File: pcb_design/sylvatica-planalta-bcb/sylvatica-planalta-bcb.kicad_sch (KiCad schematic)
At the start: 5 parts, among them J1 USB_C_Receptacle, J2 Conn_02x07_Odd_Even, J3 USB_C_Receptacle, J4 Conn_01x06

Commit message: Gerber exports
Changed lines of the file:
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@@
+    (stroke (width 0) (type default) (color 0 0 0 0))
+  )
+  (wire (pts (xy 198.12 106.68) (xy 207.01 106.68))
     (stroke (width 0) (type default) (color 0 0 0 0))
   )
@@
   )
   (wire (pts (xy 114.3 88.9) (xy 123.19 88.9))
+    (stroke (width 0) (type default) (color 0 0 0 0))
+  )
+  (wire (pts (xy 198.12 97.79) (xy 207.01 97.79))
     (stroke (width 0) (type default) (color 0 0 0 0))
   )
@@
     (pin "9")
   )
+  (symbol (lib_id "power:PWR_FLAG") (at 207.01 114.3 0) (unit 1)
+    (in_bom yes) (on_board yes) (fields_autoplaced)
+    (property "Reference" "#FLG0102" (id 0) (at 207.01 112.395 0)
+      (effects (font (size 1.27 1.27)) hide)
+    )
+    (property "Value" "PWR_FLAG" (id 1) (at 207.01 109.22 0))
+    (property "Footprint" "" (id 2) (at 207.01 114.3 0)
+      (effects (font (size 1.27 1.27)) hide)
+    )
+    (property "Datasheet" "~" (id 3) (at 207.01 114.3 0)
+      (effects (font (size 1.27 1.27)) hide)
+    )
+    (pin "1")
+  )
   (symbol (lib_id "power:VBUS") (at 123.19 83.82 0) (unit 1)
     (in_bom yes) (on_board yes) (fields_autoplaced)
@@
     )
     (property "Datasheet" "" (id 3) (at 123.19 83.82 0)
+      (effects (font (size 1.27 1.27)) hide)
+    )
+    (pin "1")
+  )
+  (symbol (lib_id "power:PWR_FLAG") (at 207.01 97.79 0) (unit 1)
+    (in_bom yes) (on_board yes) (fields_autoplaced)
+    (property "Reference" "#FLG0103" (id 0) (at 207.01 95.885 0)
+      (effects (font (size 1.27 1.27)) hide)
+    )
+    (property "Value" "PWR_FLAG" (id 1) (at 207.01 92.71 0))
+    (property "Footprint" "" (id 2) (at 207.01 97.79 0)
+      (effects (font (size 1.27 1.27)) hide)
+    )
+    (property "Datasheet" "~" (id 3) (at 207.01 97.79 0)
+      (effects (font (size 1.27 1.27)) hide)
+    )
+    (pin "1")
+  )
+  (symbol (lib_id "power:GND") (at 207.01 114.3 0) (unit 1)
+    (in_bom yes) (on_board yes) (fields_autoplaced)
+    (property "Reference" "#PWR0110" (id 0) (at 207.01 120.65 0)
+      (effects (font (size 1.27 1.27)) hide)
+    )
+    (property "Value" "GND" (id 1) (at 207.01 119.38 0))
+    (property "Footprint" "" (id 2) (at 207.01 114.3 0)
+      (effects (font (size 1.27 1.27)) hide)
+    )
+    (property "Datasheet" "" (id 3) (at 207.01 114.3 0)
       (effects (font (size 1.27 1.27)) hide)
     )
@@
     (pin "6")
   )
+  (symbol (lib_id "power:VBUS") (at 198.12 106.68 0) (unit 1)
+    (in_bom yes) (on_board yes) (fields_autoplaced)
+    (property "Reference" "#PWR0109" (id 0) (at 198.12 110.49 0)
+      (effects (font (size 1.27 1.27)) hide)
+    )
+    (property "Value" "VBUS" (id 1) (at 198.12 101.6 0))
+    (property "Footprint" "" (id 2) (at 198.12 106.68 0)
+      (effects (font (size 1.27 1.27)) hide)
+    )
+    (property "Datasheet" "" (id 3) (at 198.12 106.68 0)
+      (effects (font (size 1.27 1.27)) hide)
+    )
+    (pin "1")
+  )
   (symbol (lib_id "power:GND") (at 95.25 149.86 0) (unit 1)
     (in_bom yes) (on_board yes) (fields_autoplaced)
@@
     )
     (property "Datasheet" "" (id 3) (at 86.36 52.07 0)
+      (effects (font (size 1.27 1.27)) hide)
+    )
+    (pin "1")
+  )
+  (symbol (lib_id "power:PWR_FLAG") (at 207.01 106.68 0) (unit 1)
+    (in_bom yes) (on_board yes) (fields_autoplaced)
+    (property "Reference" "#FLG0101" (id 0) (at 207.01 104.775 0)
+      (effects (font (size 1.27 1.27)) hide)
+    )
+    (property "Value" "PWR_FLAG" (id 1) (at 207.01 101.6 0))
+    (property "Footprint" "" (id 2) (at 207.01 106.68 0)
+      (effects (font (size 1.27 1.27)) hide)
+    )
+    (property "Datasheet" "~" (id 3) (at 207.01 106.68 0)
+      (effects (font (size 1.27 1.27)) hide)
+    )
+    (pin "1")
+  )
+  (symbol (lib_id "power:+3.3V") (at 198.12 97.79 0) (unit 1)
+    (in_bom yes) (on_board yes) (fields_autoplaced)
+    (property "Reference" "#PWR0111" (id 0) (at 198.12 101.6 0)
+      (effects (font (size 1.27 1.27)) hide)
+    )
+    (property "Value" "+3.3V" (id 1) (at 198.12 92.71 0))
+    (property "Footprint" "" (id 2) (at 198.12 97.79 0)
+      (effects (font (size 1.27 1.27)) hide)
+    )
+    (property "Datasheet" "" (id 3) (at 198.12 97.79 0)
       (effects (font (size 1.27 1.27)) hide)
     )
@@
   )
   (symbol_instances
+    (path "/c01fd3c1-dfa9-46f7-a6b5-5f8ffe94637d"
+      (reference "#FLG0101") (unit 1) (value "PWR_FLAG") (footprint "")
+    )
+    (path "/73bb7407-42d7-48e9-99a3-b7d5d2bb2d1d"
+      (reference "#FLG0102") (unit 1) (value "PWR_FLAG") (footprint "")
+    )
+    (path "/93363c7c-e290-4fbd-ae52-8d881948c1c3"
+      (reference "#FLG0103") (unit 1) (value "PWR_FLAG") (footprint "")
+    )
     (path "/e31f94a3-1f71-4323-bf6e-1b3f93eeed91"
       (reference "#PWR01") (unit 1) (value "+3.3V") (footprint "")
@@
       (reference "#PWR0108") (unit 1) (value "VBUS") (footprint "")
     )
+    (path "/a5485afb-82c9-4956-9d49-d1277136f874"
+      (reference "#PWR0109") (unit 1) (value "VBUS") (footprint "")
+    )
+    (path "/941fe0bb-3818-48e0-a99d-ae1994cf3cb3"
+      (reference "#PWR0110") (unit 1) (value "GND") (footprint "")
+    )
+    (path "/c4b96c0e-e6e5-4d46-8fac-385633c2366c"
+      (reference "#PWR0111") (unit 1) (value "+3.3V") (footprint "")
+    )
     (path "/dc37d966-d882-4451-ba5d-342ef3a9987e"

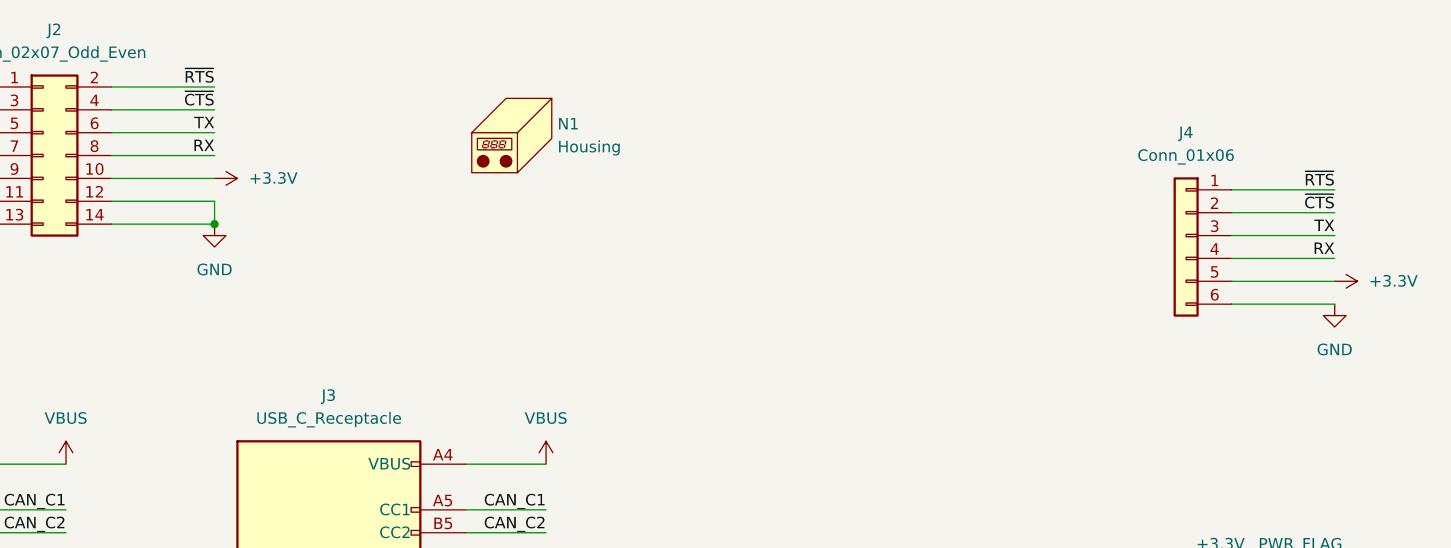
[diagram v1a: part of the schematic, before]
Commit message: Expose RTCC pin for synchronisation
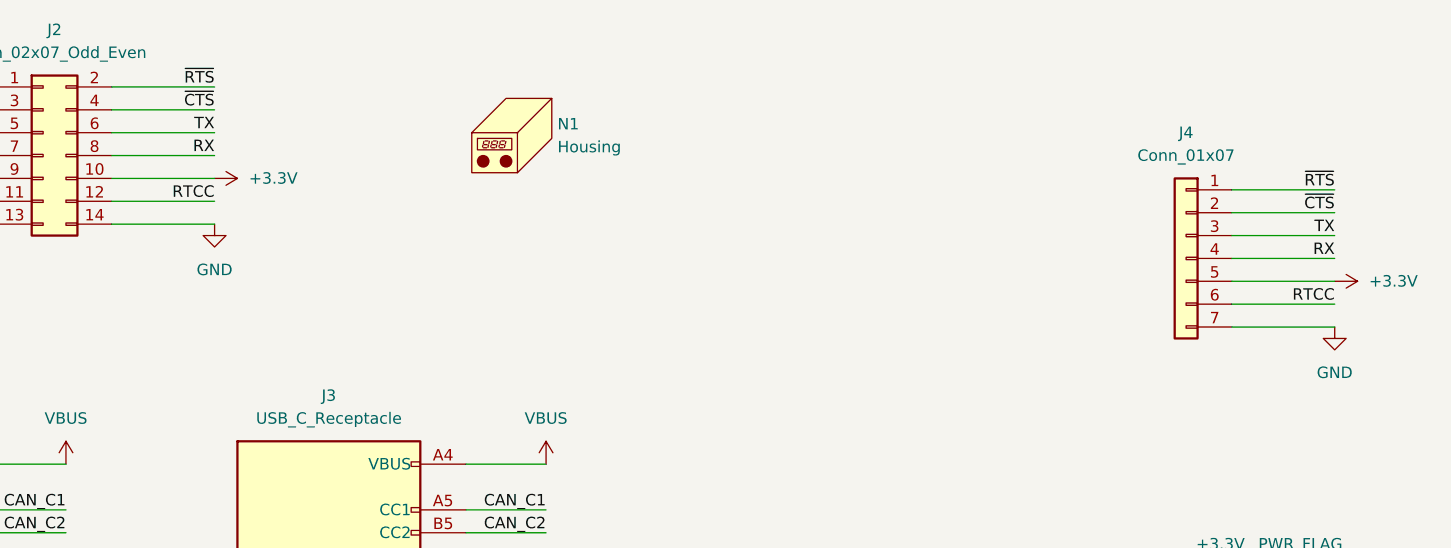
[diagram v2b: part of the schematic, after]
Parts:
- removed J4: Conn_01x06, Connector_PinHeader_2.54mm:PinHeader_1x06_P2.54mm_Vertical, symbol Connector_Generic:Conn_01x06
- added J4: Conn_01x07, Connector_PinHeader_2.54mm:PinHeader_1x07_P2.54mm_Vertical, symbol Connector_Generic:Conn_01x07
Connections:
- net +3.3V: now also J4.5 (Pin_5)
- net GND: now also J4.7 (Pin_7); no longer J2.12 (Pin_12)
- net RX: now also J4.4 (Pin_4)
- net TX: now also J4.3 (Pin_3)
- net ~{CTS}: now also J4.2 (Pin_2)
- net ~{RTS}: now also J4.1 (Pin_1)
- new net RTCC: J2.12 (Pin_12), J4.6 (Pin_6)
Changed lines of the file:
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@@
   (junction (at 41.91 149.86) (diameter 0) (color 0 0 0 0)
-  )
-  (junction (at 86.36 57.15) (diameter 0) (color 0 0 0 0)
   )
   (no_connect (at 114.3 124.46))
@@
     (stroke (width 0) (type default) (color 0 0 0 0))
   )
-  (wire (pts (xy 86.36 54.61) (xy 86.36 57.15))
-    (stroke (width 0) (type default) (color 0 0 0 0))
-  )
   (wire (pts (xy 199.39 55.88) (xy 210.82 55.88))
     (stroke (width 0) (type default) (color 0 0 0 0))
@@
     (stroke (width 0) (type default) (color 0 0 0 0))
   )
-  (wire (pts (xy 210.82 66.04) (xy 199.39 66.04))
+  (wire (pts (xy 210.82 68.58) (xy 199.39 68.58))
     (stroke (width 0) (type default) (color 0 0 0 0))
   )
@@
   )
   (wire (pts (xy 50.8 46.99) (xy 62.23 46.99))
+    (stroke (width 0) (type default) (color 0 0 0 0))
+  )
+  (wire (pts (xy 199.39 66.04) (xy 210.82 66.04))
     (stroke (width 0) (type default) (color 0 0 0 0))
   )
@@
     (effects (font (size 1.27 1.27)) (justify right bottom))
   )
+  (label "RTCC" (at 86.36 54.61 180)
+    (effects (font (size 1.27 1.27)) (justify right bottom))
+  )
   (label "CAN_H" (at 123.19 101.6 180)
     (effects (font (size 1.27 1.27)) (justify right bottom))
   )
   (label "CAN_H" (at 69.85 104.14 180)
+    (effects (font (size 1.27 1.27)) (justify right bottom))
+  )
+  (label "RTCC" (at 210.82 66.04 180)
     (effects (font (size 1.27 1.27)) (justify right bottom))
   )
@@
     )
     (pin "1")
+  )
+  (symbol (lib_id "Connector_Generic:Conn_01x07") (at 194.31 60.96 0) (mirror y) (unit 1)
+    (in_bom yes) (on_board yes) (fields_autoplaced)
+    (property "Reference" "J4" (id 0) (at 194.31 46.99 0))
+    (property "Value" "Conn_01x07" (id 1) (at 194.31 49.53 0))
+    (property "Footprint" "Connector_PinHeader_2.54mm:PinHeader_1x07_P2.54mm_Vertical" (id 2) (at 194.31 60.96 0)
+      (effects (font (size 1.27 1.27)) hide)
+    )
+    (property "Datasheet" "~" (id 3) (at 194.31 60.96 0)
+      (effects (font (size 1.27 1.27)) hide)
+    )
+    (pin "1")
+    (pin "2")
+    (pin "3")
+    (pin "4")
+    (pin "5")
+    (pin "6")
+    (pin "7")
   )
   (symbol (lib_id "power:GND") (at 41.91 149.86 0) (unit 1)
@@
     (pin "1")
   )
-  (symbol (lib_id "power:GND") (at 210.82 66.04 0) (mirror y) (unit 1)
-    (in_bom yes) (on_board yes) (fields_autoplaced)
-    (property "Reference" "#PWR02" (id 0) (at 210.82 72.39 0)
-      (effects (font (size 1.27 1.27)) hide)
-    )
-    (property "Value" "GND" (id 1) (at 210.82 71.12 0))
-    (property "Footprint" "" (id 2) (at 210.82 66.04 0)
-      (effects (font (size 1.27 1.27)) hide)
-    )
-    (property "Datasheet" "" (id 3) (at 210.82 66.04 0)
-      (effects (font (size 1.27 1.27)) hide)
-    )
-    (pin "1")
-  )
-  (symbol (lib_id "Connector_Generic:Conn_01x06") (at 194.31 58.42 0) (mirror y) (unit 1)
-    (in_bom yes) (on_board yes) (fields_autoplaced)
-    (property "Reference" "J4" (id 0) (at 194.31 46.99 0))
-    (property "Value" "Conn_01x06" (id 1) (at 194.31 49.53 0))
-    (property "Footprint" "Connector_PinHeader_2.54mm:PinHeader_1x06_P2.54mm_Vertical" (id 2) (at 194.31 58.42 0)
-      (effects (font (size 1.27 1.27)) hide)
-    )
-    (property "Datasheet" "~" (id 3) (at 194.31 58.42 0)
-      (effects (font (size 1.27 1.27)) hide)
-    )
-    (pin "1")
-    (pin "2")
-    (pin "3")
-    (pin "4")
-    (pin "5")
-    (pin "6")
+  (symbol (lib_id "power:GND") (at 210.82 68.58 0) (mirror y) (unit 1)
+    (in_bom yes) (on_board yes) (fields_autoplaced)
+    (property "Reference" "#PWR02" (id 0) (at 210.82 74.93 0)
+      (effects (font (size 1.27 1.27)) hide)
+    )
+    (property "Value" "GND" (id 1) (at 210.82 73.66 0))
+    (property "Footprint" "" (id 2) (at 210.82 68.58 0)
+      (effects (font (size 1.27 1.27)) hide)
+    )
+    (property "Datasheet" "" (id 3) (at 210.82 68.58 0)
+      (effects (font (size 1.27 1.27)) hide)
+    )
+    (pin "1")
   )
   (symbol (lib_id "power:VBUS") (at 198.12 106.68 0) (unit 1)
@@
       (reference "J3") (unit 1) (value "USB_C_Receptacle") (footprint "custom_footprints:USB_C_Receptacle_Amphenol_12401861XX12A")
     )
-    (path "/9b7e35f5-486c-4f92-a9e6-663f833ed527"
-      (reference "J4") (unit 1) (value "Conn_01x06") (footprint "Connector_PinHeader_2.54mm:PinHeader_1x06_P2.54mm_Vertical")
+    (path "/48d00e43-6860-403b-b840-ae8499bf2a26"
+      (reference "J4") (unit 1) (value "Conn_01x07") (footprint "Connector_PinHeader_2.54mm:PinHeader_1x07_P2.54mm_Vertical")
     )
     (path "/5a76c744-ee33-44cc-b6c5-ae766ea68974"

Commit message: Various updates for Aisler order.
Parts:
- J1, J3: MPN (none) -> 124018612112A; Manufacturer (none) -> Amphenol
- J2: MPN (none) -> MMS-107-02-F-DV; Manufacturer (none) -> Samtec
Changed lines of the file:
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@@
+      (effects (font (size 1.27 1.27)) hide)
+    )
+    (property "MPN" "MMS-107-02-F-DV" (id 4) (at 67.31 49.53 0)
+      (effects (font (size 1.27 1.27)) hide)
+    )
+    (property "Manufacturer" "Samtec" (id 5) (at 67.31 49.53 0)
       (effects (font (size 1.27 1.27)) hide)
     )
@@
     )
     (property "Datasheet" "https://www.usb.org/sites/default/files/documents/usb_type-c.zip" (id 3) (at 49.53 109.22 0)
+      (effects (font (size 1.27 1.27)) hide)
+    )
+    (property "MPN" "124018612112A" (id 4) (at 45.72 109.22 0)
+      (effects (font (size 1.27 1.27)) hide)
+    )
+    (property "Manufacturer" "Amphenol" (id 5) (at 45.72 109.22 0)
       (effects (font (size 1.27 1.27)) hide)
     )
@@
       (effects (font (size 1.27 1.27)) hide)
     )
+    (property "MPN" "124018612112A" (id 4) (at 99.06 109.22 0)
+      (effects (font (size 1.27 1.27)) hide)
+    )
+    (property "Manufacturer" "Amphenol" (id 5) (at 99.06 109.22 0)
+      (effects (font (size 1.27 1.27)) hide)
+    )
